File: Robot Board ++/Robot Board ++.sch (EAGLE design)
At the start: 128 parts, among them U10 74XX125.RGY, U11 SCHA4B0400, U12 BLUETOOTH-RN41", U13 XBEE-1XBEE-1_LOCK, U5 TPS5331[8/9].DQP, U6 TPS62082.DSG, U7 PCA9557.RGV, U8 MPU-6050, U9 ADS7830.PW

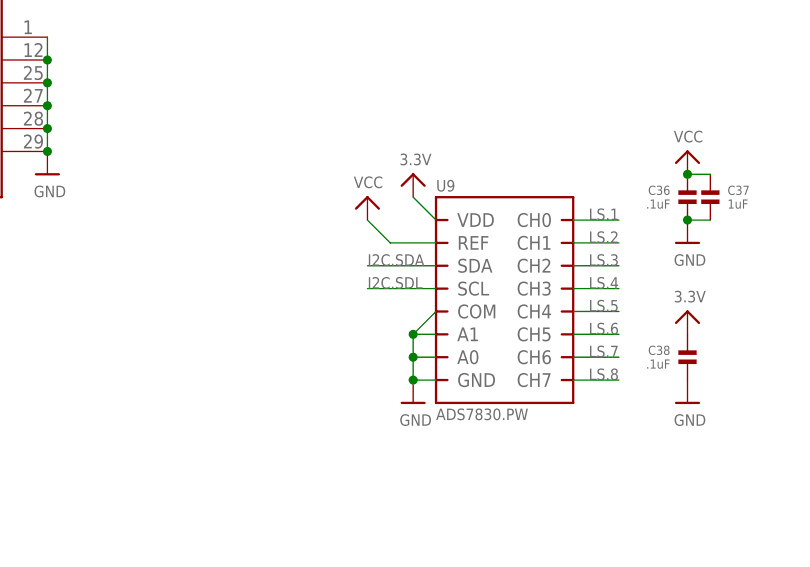
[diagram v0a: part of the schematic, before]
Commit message: Routing fun! Redrawing ratsnest is now taking a measurable amount of time...
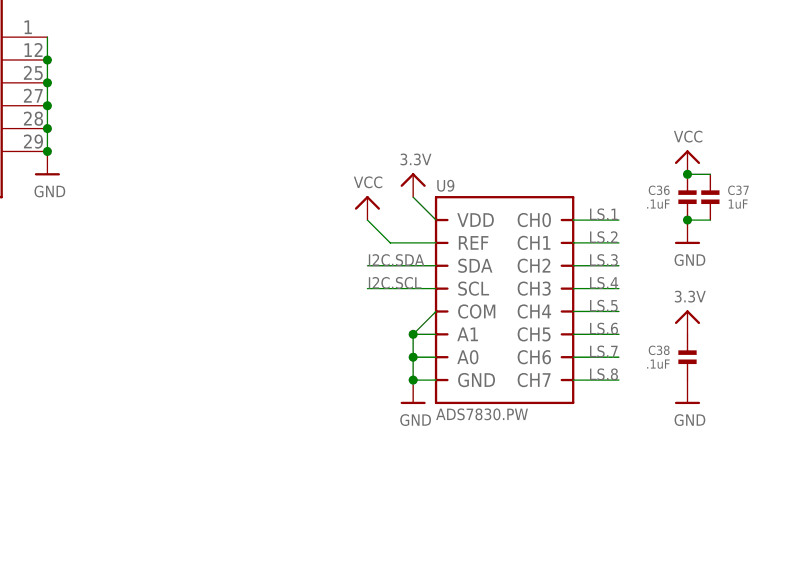
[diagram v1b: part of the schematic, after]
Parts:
- J5, J6, J7, J8: device solderjumper:SOLDERJUMPER.2.MED -> solderjumper:SOLDERJUMPER.2.LRG
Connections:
- removed net I2C.SDL: U9.SCL
- net I2C.SCL: now also U9.SCL
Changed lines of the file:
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@@
 <grid distance="0.1" unitdist="inch" unit="inch" style="lines" multiple="1" display="no" altdistance="0.01" altunitdist="inch" altunit="inch"/>
 <layers>
-<layer number="1" name="Top" color="4" fill="1" visible="no" active="no"/>
-<layer number="2" name="Route2" color="1" fill="3" visible="no" active="no"/>
-<layer number="3" name="Route3" color="4" fill="3" visible="no" active="no"/>
-<layer number="4" name="Route4" color="1" fill="4" visible="no" active="no"/>
-<layer number="5" name="Route5" color="4" fill="4" visible="no" active="no"/>
-<layer number="6" name="Route6" color="1" fill="8" visible="no" active="no"/>
-<layer number="7" name="Route7" color="4" fill="8" visible="no" active="no"/>
-<layer number="8" name="Route8" color="1" fill="2" visible="no" active="no"/>
-<layer number="9" name="Route9" color="4" fill="2" visible="no" active="no"/>
-<layer number="10" name="Route10" color="1" fill="7" visible="no" active="no"/>
-<layer number="11" name="Route11" color="4" fill="7" visible="no" active="no"/>
-<layer number="12" name="Route12" color="1" fill="5" visible="no" active="no"/>
-<layer number="13" name="Route13" color="4" fill="5" visible="no" active="no"/>
-<layer number="14" name="Route14" color="1" fill="6" visible="no" active="no"/>
-<layer number="15" name="Route15" color="4" fill="6" visible="no" active="no"/>
-<layer number="16" name="Bottom" color="1" fill="1" visible="no" active="no"/>
-<layer number="17" name="Pads" color="2" fill="1" visible="no" active="no"/>
-<layer number="18" name="Vias" color="2" fill="1" visible="no" active="no"/>
-<layer number="19" name="Unrouted" color="6" fill="1" visible="no" active="no"/>
-<layer number="20" name="Dimension" color="15" fill="1" visible="no" active="no"/>
-<layer number="21" name="tPlace" color="7" fill="1" visible="no" active="no"/>
-<layer number="22" name="bPlace" color="7" fill="1" visible="no" active="no"/>
-<layer number="23" name="tOrigins" color="15" fill="1" visible="no" active="no"/>
-<layer number="24" name="bOrigins" color="15" fill="1" visible="no" active="no"/>
-<layer number="25" name="tNames" color="7" fill="1" visible="no" active="no"/>
-<layer number="26" name="bNames" color="7" fill="1" visible="no" active="no"/>
-<layer number="27" name="tValues" color="7" fill="1" visible="no" active="no"/>
-<layer number="28" name="bValues" color="7" fill="1" visible="no" active="no"/>
+<layer number="1" name="Top" color="4" fill="1" visible="yes" active="no"/>
+<layer number="2" name="Route2" color="1" fill="3" visible="yes" active="no"/>
+<layer number="3" name="Route3" color="4" fill="3" visible="yes" active="no"/>
+<layer number="4" name="Route4" color="1" fill="4" visible="yes" active="no"/>
+<layer number="5" name="Route5" color="4" fill="4" visible="yes" active="no"/>
+<layer number="6" name="Route6" color="1" fill="8" visible="yes" active="no"/>
+<layer number="7" name="Route7" color="4" fill="8" visible="yes" active="no"/>
+<layer number="8" name="Route8" color="1" fill="2" visible="yes" active="no"/>
+<layer number="9" name="Route9" color="4" fill="2" visible="yes" active="no"/>
+<layer number="10" name="Route10" color="1" fill="7" visible="yes" active="no"/>
+<layer number="11" name="Route11" color="4" fill="7" visible="yes" active="no"/>
+<layer number="12" name="Route12" color="1" fill="5" visible="yes" active="no"/>
+<layer number="13" name="Route13" color="4" fill="5" visible="yes" active="no"/>
+<layer number="14" name="Route14" color="1" fill="6" visible="yes" active="no"/>
+<layer number="15" name="Route15" color="4" fill="6" visible="yes" active="no"/>
+<layer number="16" name="Bottom" color="1" fill="1" visible="yes" active="no"/>
+<layer number="17" name="Pads" color="2" fill="1" visible="yes" active="no"/>
+<layer number="18" name="Vias" color="2" fill="1" visible="yes" active="no"/>
+<layer number="19" name="Unrouted" color="6" fill="1" visible="yes" active="no"/>
+<layer number="20" name="Dimension" color="15" fill="1" visible="yes" active="no"/>
+<layer number="21" name="tPlace" color="7" fill="1" visible="yes" active="no"/>
+<layer number="22" name="bPlace" color="7" fill="1" visible="yes" active="no"/>
+<layer number="23" name="tOrigins" color="15" fill="1" visible="yes" active="no"/>
+<layer number="24" name="bOrigins" color="15" fill="1" visible="yes" active="no"/>
+<layer number="25" name="tNames" color="7" fill="1" visible="yes" active="no"/>
+<layer number="26" name="bNames" color="7" fill="1" visible="yes" active="no"/>
+<layer number="27" name="tValues" color="7" fill="1" visible="yes" active="no"/>
+<layer number="28" name="bValues" color="7" fill="1" visible="yes" active="no"/>
 <layer number="29" name="tStop" color="7" fill="3" visible="no" active="no"/>
 <layer number="30" name="bStop" color="7" fill="6" visible="no" active="no"/>
@@
 <layer number="35" name="tGlue" color="7" fill="4" visible="no" active="no"/>
 <layer number="36" name="bGlue" color="7" fill="5" visible="no" active="no"/>
-<layer number="37" name="tTest" color="7" fill="1" visible="no" active="no"/>
-<layer number="38" name="bTest" color="7" fill="1" visible="no" active="no"/>
+<layer number="37" name="tTest" color="7" fill="1" visible="yes" active="no"/>
+<layer number="38" name="bTest" color="7" fill="1" visible="yes" active="no"/>
 <layer number="39" name="tKeepout" color="4" fill="11" visible="no" active="no"/>
 <layer number="40" name="bKeepout" color="1" fill="11" visible="no" active="no"/>
@@
 <layer number="44" name="Drills" color="7" fill="1" visible="no" active="no"/>
 <layer number="45" name="Holes" color="7" fill="1" visible="no" active="no"/>
-<layer number="46" name="Milling" color="3" fill="1" visible="no" active="no"/>
-<layer number="47" name="Measures" color="7" fill="1" visible="no" active="no"/>
-<layer number="48" name="Document" color="7" fill="1" visible="no" active="no"/>
-<layer number="49" name="Reference" color="7" fill="1" visible="no" active="no"/>
-<layer number="50" name="dxf" color="7" fill="1" visible="no" active="no"/>
-<layer number="51" name="tDocu" color="7" fill="1" visible="no" active="no"/>
-<layer number="52" name="bDocu" color="7" fill="1" visible="no" active="no"/>
-<layer number="53" name="tGND_GNDA" color="7" fill="9" visible="no" active="no"/>
-<layer number="54" name="bGND_GNDA" color="1" fill="9" visible="no" active="no"/>
-<layer number="56" name="wert" color="7" fill="1" visible="no" active="no"/>
-<layer number="59" name="tCarbon" color="7" fill="1" visible="no" active="no"/>
-<layer number="60" name="bCarbon" color="7" fill="1" visible="no" active="no"/>
+<layer number="46" name="Milling" color="3" fill="1" visible="yes" active="no"/>
+<layer number="47" name="Measures" color="7" fill="1" visible="yes" active="no"/>
+<layer number="48" name="Document" color="7" fill="1" visible="yes" active="no"/>
+<layer number="49" name="Reference" color="7" fill="1" visible="yes" active="no"/>
+<layer number="50" name="dxf" color="7" fill="1" visible="yes" active="no"/>
+<layer number="51" name="tDocu" color="7" fill="1" visible="yes" active="no"/>
+<layer number="52" name="bDocu" color="7" fill="1" visible="yes" active="no"/>
+<layer number="53" name="tGND_GNDA" color="7" fill="9" visible="yes" active="no"/>
+<layer number="54" name="bGND_GNDA" color="1" fill="9" visible="yes" active="no"/>
+<layer number="56" name="wert" color="7" fill="1" visible="yes" active="no"/>
+<layer number="59" name="tCarbon" color="7" fill="1" visible="yes" active="no"/>
+<layer number="60" name="bCarbon" color="7" fill="1" visible="yes" active="no"/>
 <layer number="91" name="Nets" color="2" fill="1" visible="yes" active="yes"/>
 <layer number="92" name="Busses" color="1" fill="1" visible="yes" active="yes"/>
@@
 <part name="J3" library="solderjumper" deviceset="SOLDERJUMPER.2" device=".XL"/>
 <part name="J4" library="solderjumper" deviceset="SOLDERJUMPER.2" device=".XL"/>
-<part name="J5" library="solderjumper" deviceset="SOLDERJUMPER.2" device=".MED"/>
-<part name="J6" library="solderjumper" deviceset="SOLDERJUMPER.2" device=".MED"/>
-<part name="J7" library="solderjumper" deviceset="SOLDERJUMPER.2" device=".MED"/>
-<part name="J8" library="solderjumper" deviceset="SOLDERJUMPER.2" device=".MED"/>
+<part name="J5" library="solderjumper" deviceset="SOLDERJUMPER.2" device=".LRG"/>
+<part name="J6" library="solderjumper" deviceset="SOLDERJUMPER.2" device=".LRG"/>
+<part name="J7" library="solderjumper" deviceset="SOLDERJUMPER.2" device=".LRG"/>
+<part name="J8" library="solderjumper" deviceset="SOLDERJUMPER.2" device=".LRG"/>
 <part name="C16" library="microbuilder" deviceset="CAP_ELECTROLYTIC" device="PANASONIC_C" value="100uF"/>
 <part name="C18" library="microbuilder" deviceset="CAP_ELECTROLYTIC" device="PANASONIC_C" value="100uF"/>
@@
 <label x="195.58" y="10.16" size="1.27" layer="95" rot="MR0"/>
 </segment>
+<segment>
+<pinref part="U9" gate="G$1" pin="SCL"/>
+<wire x1="231.14" y1="167.64" x2="223.52" y2="167.64" width="0.1524" layer="91"/>
+<label x="223.52" y="167.64" size="1.27" layer="95"/>
+</segment>
 </net>
 <net name="UART.RXI" class="0">
@@
 </segment>
 </net>
-<net name="I2C.SDL" class="0">
-<segment>
-<pinref part="U9" gate="G$1" pin="SCL"/>
-<wire x1="231.14" y1="167.64" x2="223.52" y2="167.64" width="0.1524" layer="91"/>
-<label x="223.52" y="167.64" size="1.27" layer="95"/>
-</segment>
-</net>

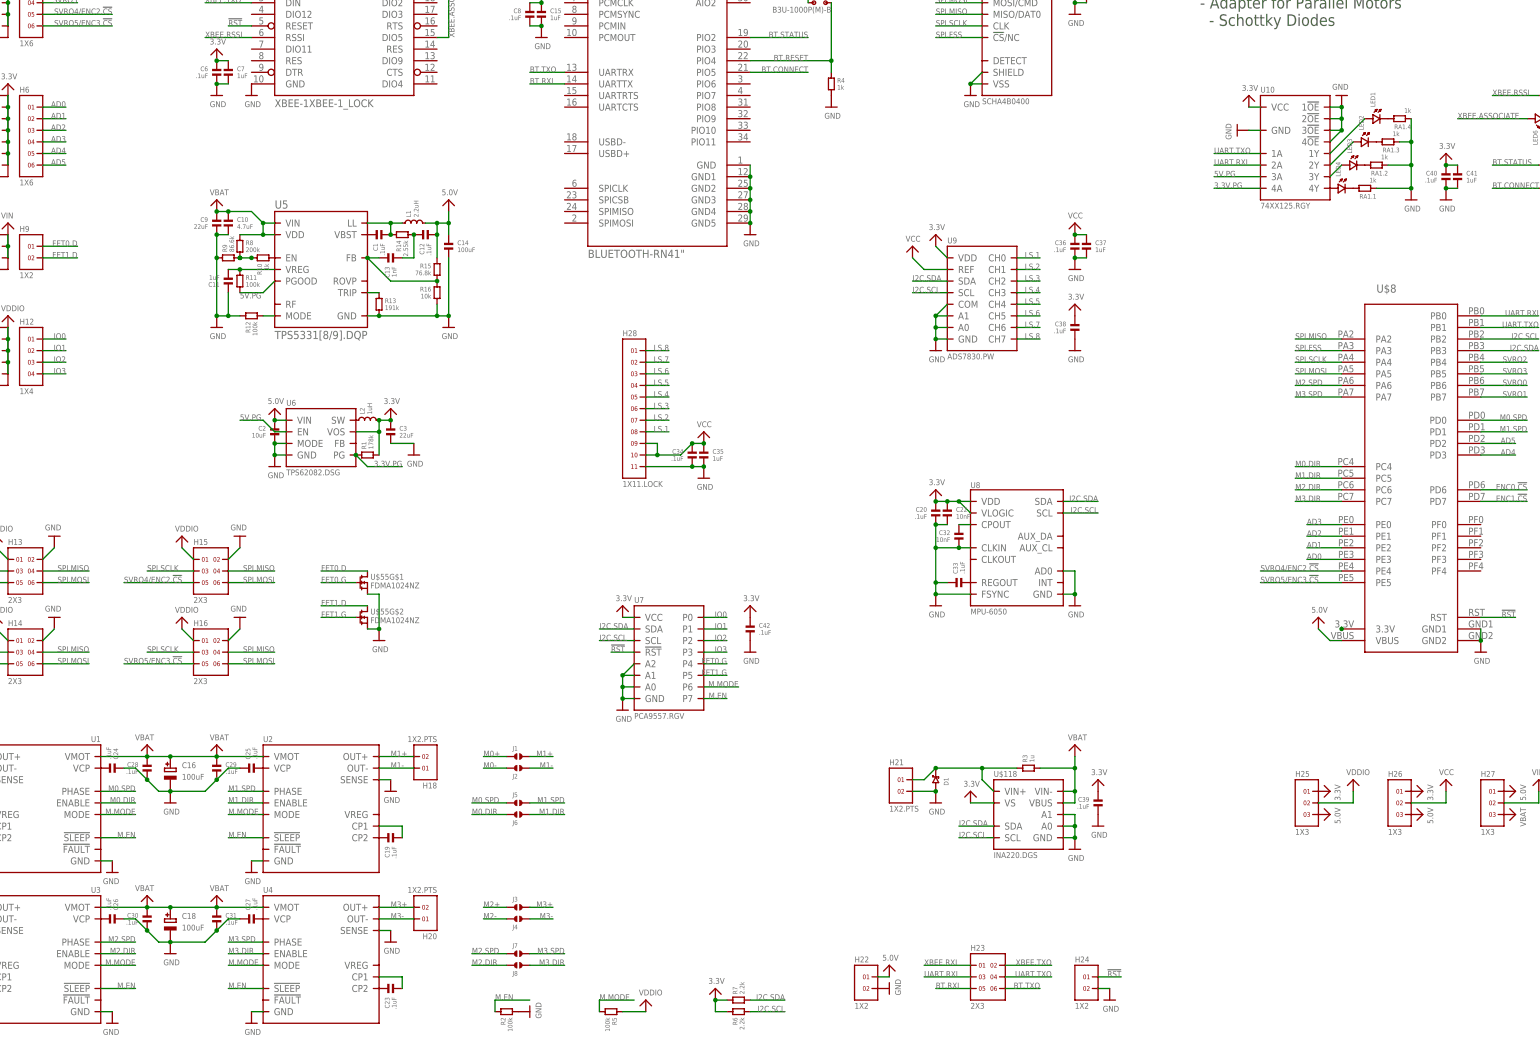
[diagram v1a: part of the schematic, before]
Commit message: Removed Line Sensor breakout. Replaced with I2C and UART breakout pins Will need to create an I2C to ADC breakout board sometime in the future...
That line sensor connector was the worst...
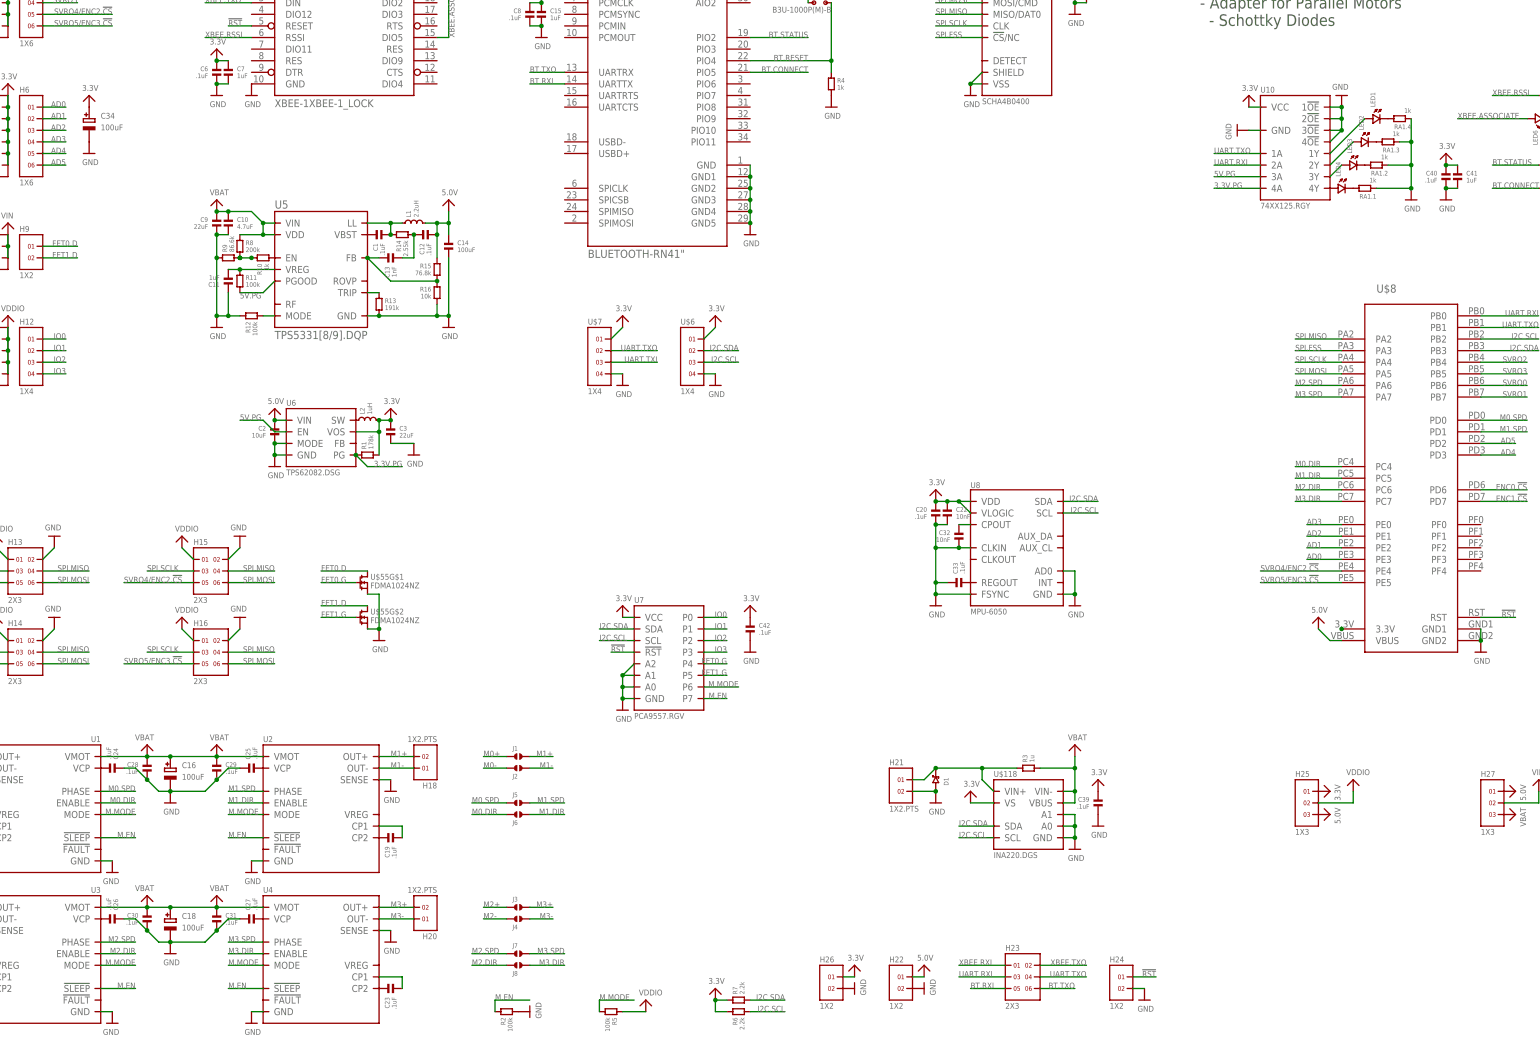
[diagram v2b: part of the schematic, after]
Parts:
- removed C35, C37: 1uF, standardparts:CAPACITOR.0603
- removed C36, C38: .1uF, standardparts:CAPACITOR.0603
- removed H28: 1X11.LOCK, headers(.1in):1X11.LOCK
- removed U9: ADS7830.PW, packages(ti):ADS7830.PW
- added U$6, U$7: 1X4, headers(.1in):1X4
- C34: value .1uF -> 100uF; device standardparts:CAPACITOR.0603 -> microbuilder:CAP_ELECTROLYTICPANASONIC_C
- H26: value 1X3 -> 1X2; device headers(2mm):1X3 -> headers(.1in):1X2
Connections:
- removed net LS.1: H28.8, U9.CH0
- removed net LS.2: H28.7, U9.CH1
- removed net LS.3: H28.6, U9.CH2
- removed net LS.4: H28.5, U9.CH3
- removed net LS.5: H28.4, U9.CH4
- removed net LS.6: H28.3, U9.CH5
- removed net LS.7: H28.2, U9.CH6
- removed net LS.8: H28.1, U9.CH7
- removed net VCC: C34.1, C35.1, C36.1, C37.1, H26.2, H28.10, H28.9, U9.REF
- new net UART.TXI: U$7.3
- net 3.3V: now also C34.+, U$6.1, U$7.1; no longer C38.1, U9.VDD
- net 5.0V: no longer H26.3
- net GND: now also C34.-, H26.2, U$6.4, U$7.4; no longer C34.2, C35.2, C36.2, C37.2, C38.2, H28.11, U9.A0, U9.A1, U9.COM, U9.GND
- net I2C.SCL: now also U$6.3; no longer U9.SCL
- net I2C.SDA: now also U$6.2; no longer U9.SDA
- net UART.TXO: now also U$7.2
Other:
- moved on the sheet: H22, H23, H24
